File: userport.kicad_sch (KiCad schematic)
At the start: 43 parts, among them J3 C64_User_Port, J4 Mini-DIN-8-With-Shield, J5 C64_Tape_Port, J6 OKR-T/3-W12-C, U1 74LS595, U10 74LS125, U11 74LS595, U2 74LVC165, U3 74LS125, U4 74LS595, U5 74LVC165, U6 74LS595, U7 74LVC165, U8 74LS125, U9 74LS125

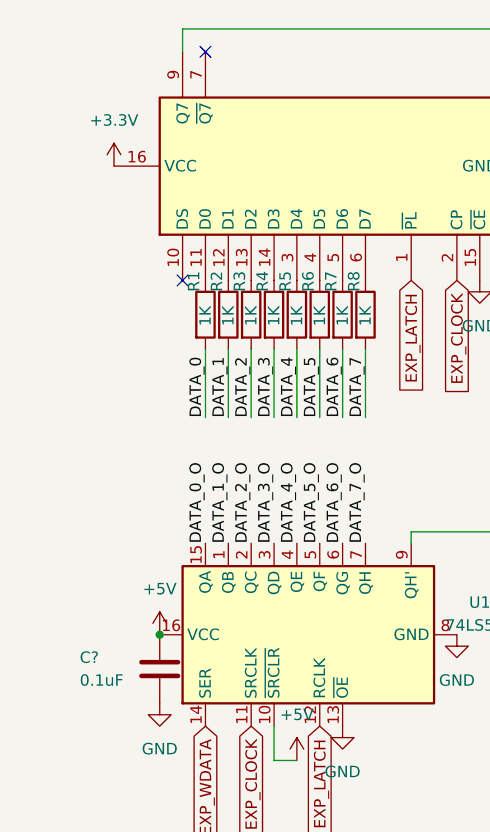
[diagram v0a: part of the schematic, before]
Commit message: add decoupling cap to U2
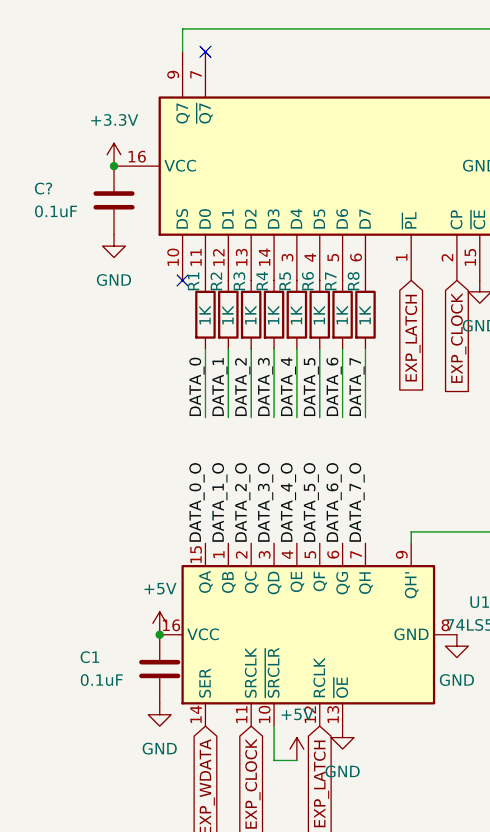
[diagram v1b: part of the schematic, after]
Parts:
- added C?: 0.1uF, Capacitor_THT:C_Disc_D5.0mm_W2.5mm_P5.00mm, symbol Device:C
- C1: renamed from C?; footprint Capacitor_THT:C_Disc_D10.0mm_W2.5mm_P5.00mm -> Capacitor_THT:C_Disc_D5.0mm_W2.5mm_P5.00mm
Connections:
- net +3V3: now also C?.1
- net GND: now also C?.2

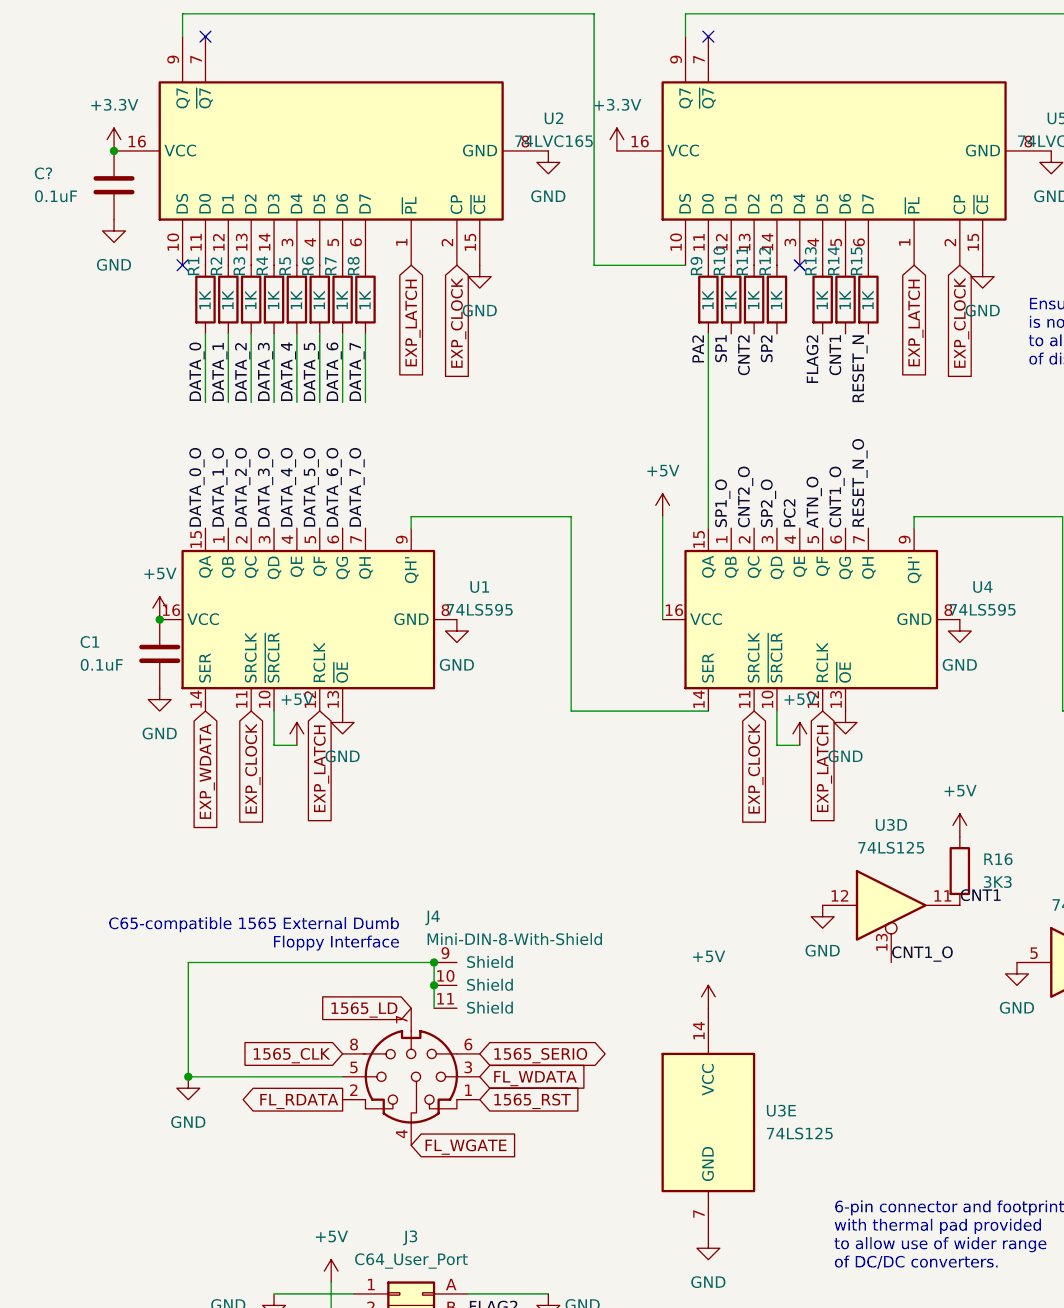
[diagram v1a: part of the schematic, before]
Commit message: add decoupling cap to U3
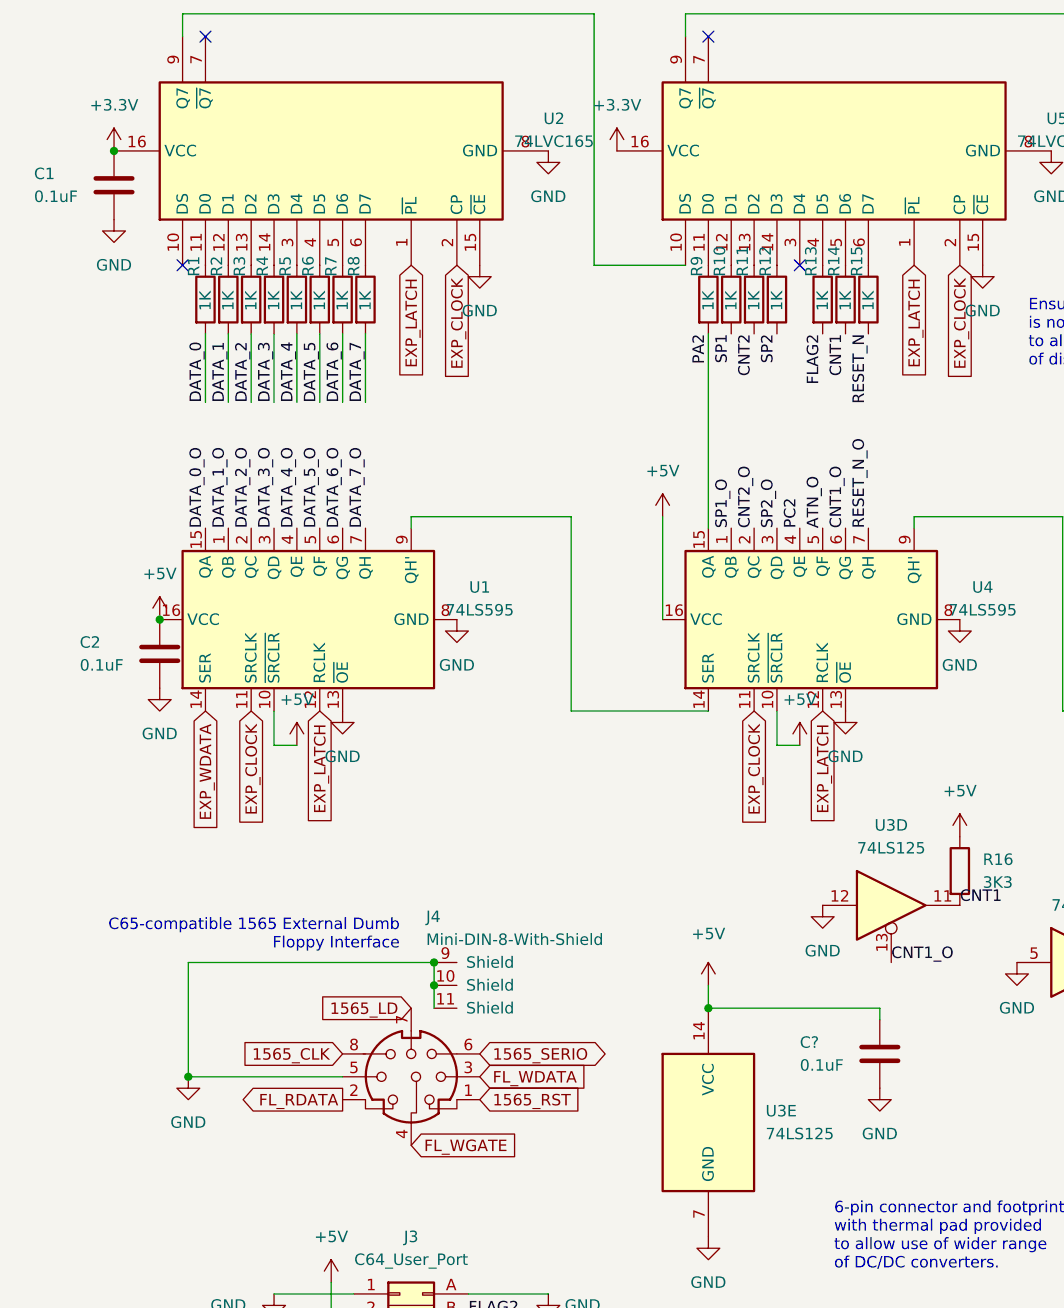
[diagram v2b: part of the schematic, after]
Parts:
- added C?: 0.1uF, Capacitor_THT:C_Disc_D5.0mm_W2.5mm_P5.00mm, symbol Device:C
- gave numbers to parts that had none: 1
- renumbered C1 to C2
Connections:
- net +5V: now also C?.1
- net GND: now also C?.2

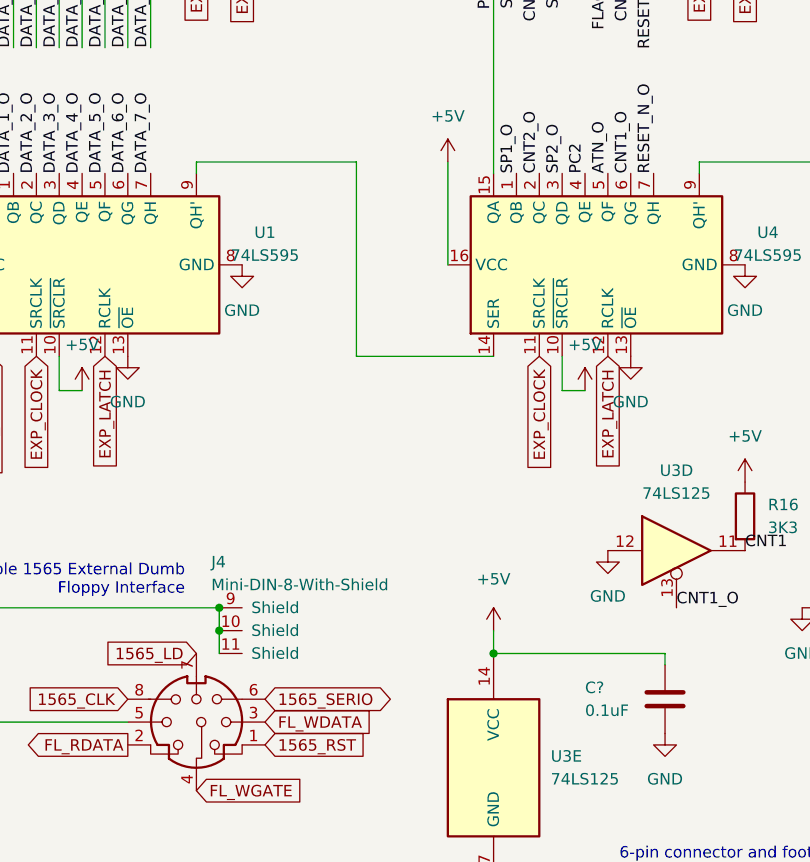
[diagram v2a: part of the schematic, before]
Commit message: add decoupling cap to U4
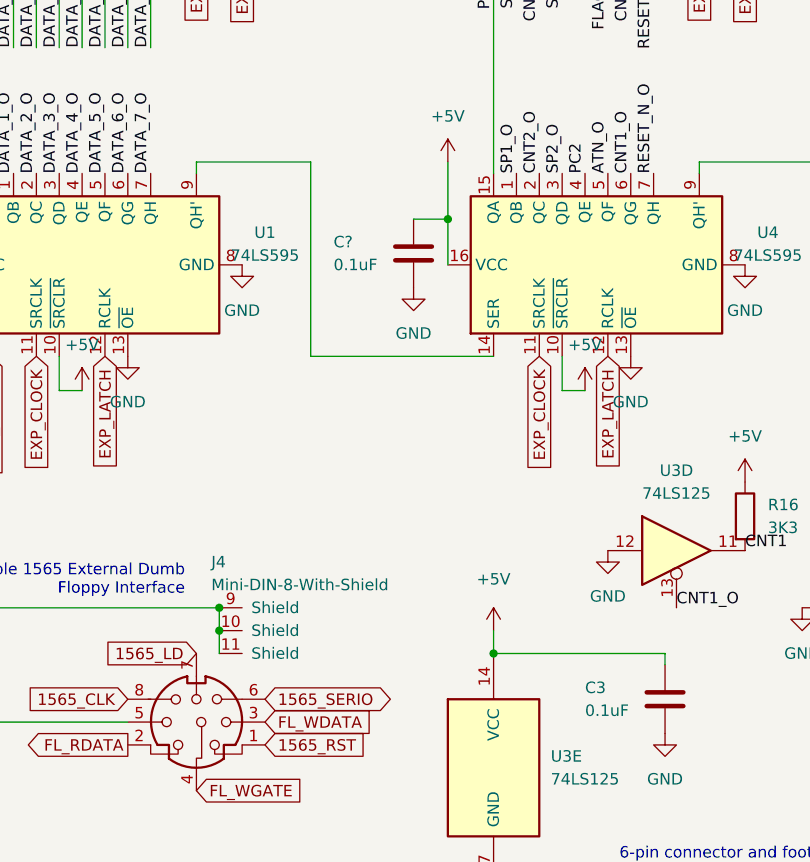
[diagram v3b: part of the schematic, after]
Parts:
- added C?: 0.1uF, Capacitor_THT:C_Disc_D5.0mm_W2.5mm_P5.00mm, symbol Device:C
- gave numbers to parts that had none: 1
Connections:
- net +5V: now also C?.1
- net GND: now also C?.2

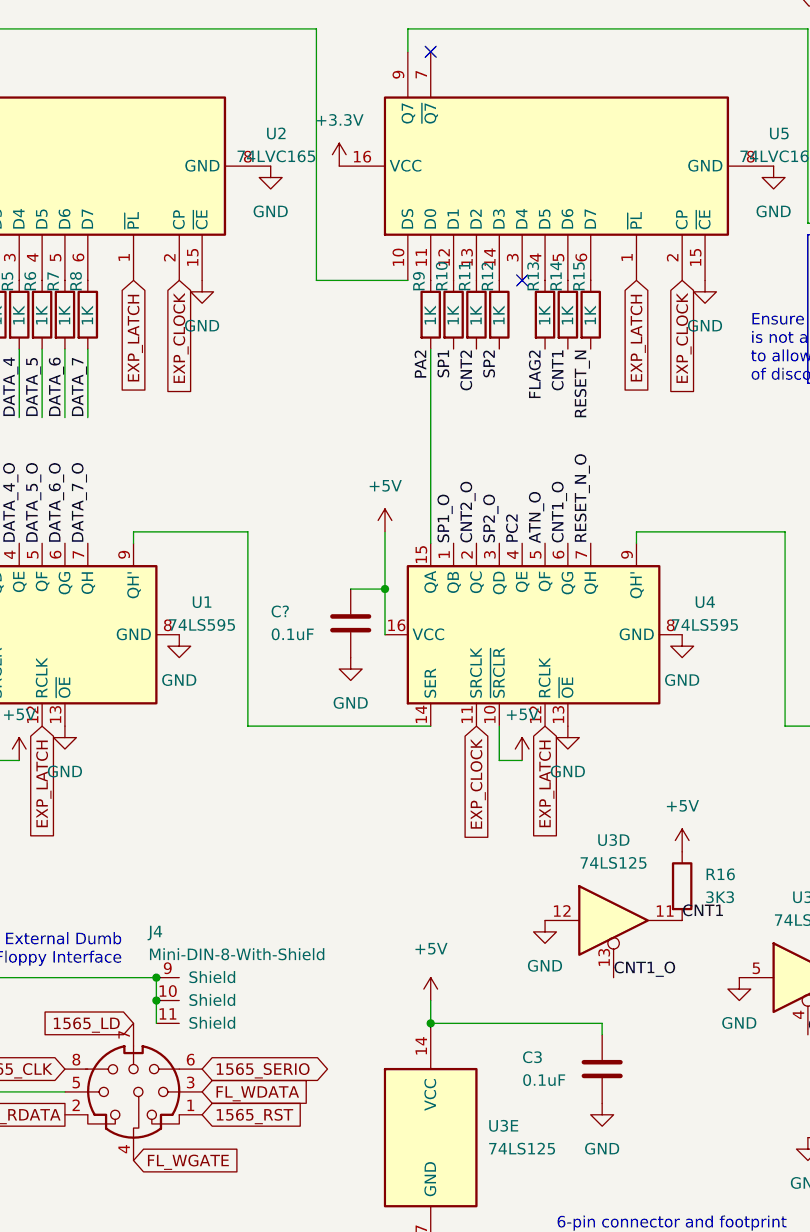
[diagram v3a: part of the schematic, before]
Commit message: add decoupling cap to U5
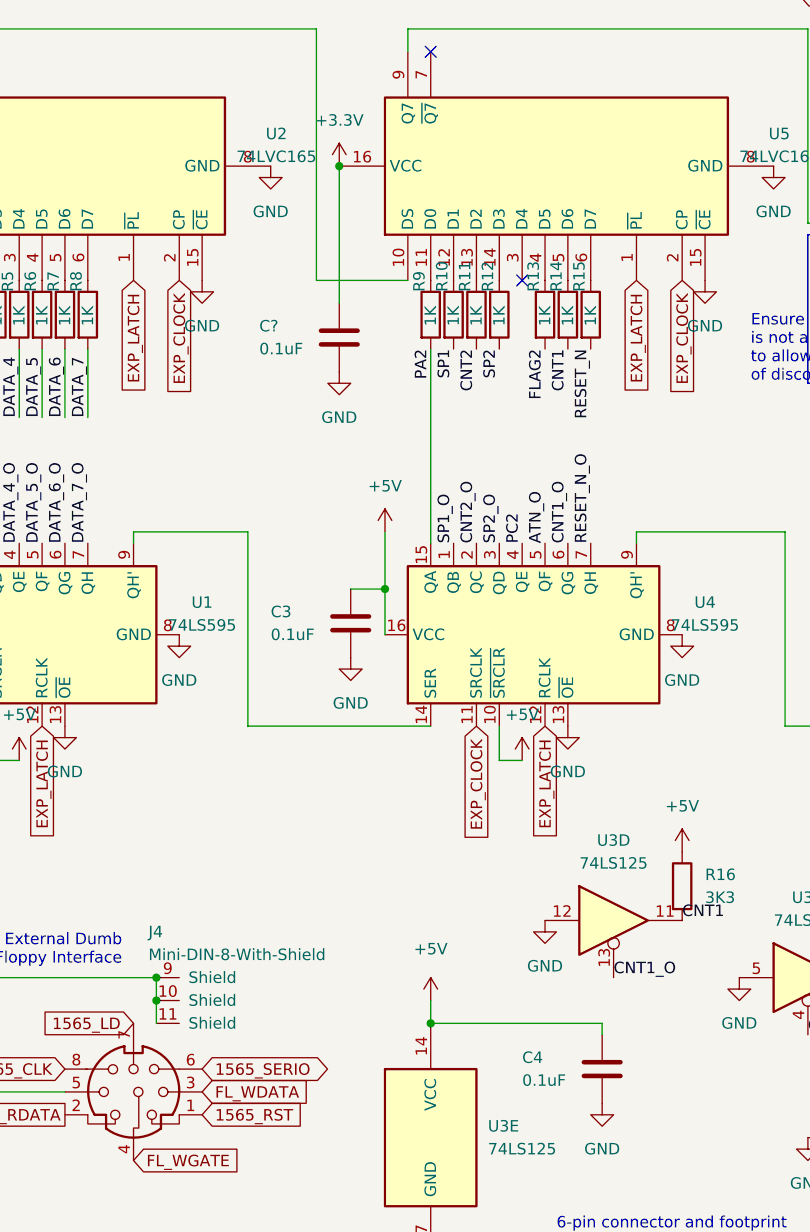
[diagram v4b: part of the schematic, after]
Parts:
- added C?: 0.1uF, Capacitor_THT:C_Disc_D5.0mm_W2.5mm_P5.00mm, symbol Device:C
- gave numbers to parts that had none: 1
- renumbered C3 to C4
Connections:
- net +3V3: now also C?.1
- net GND: now also C?.2

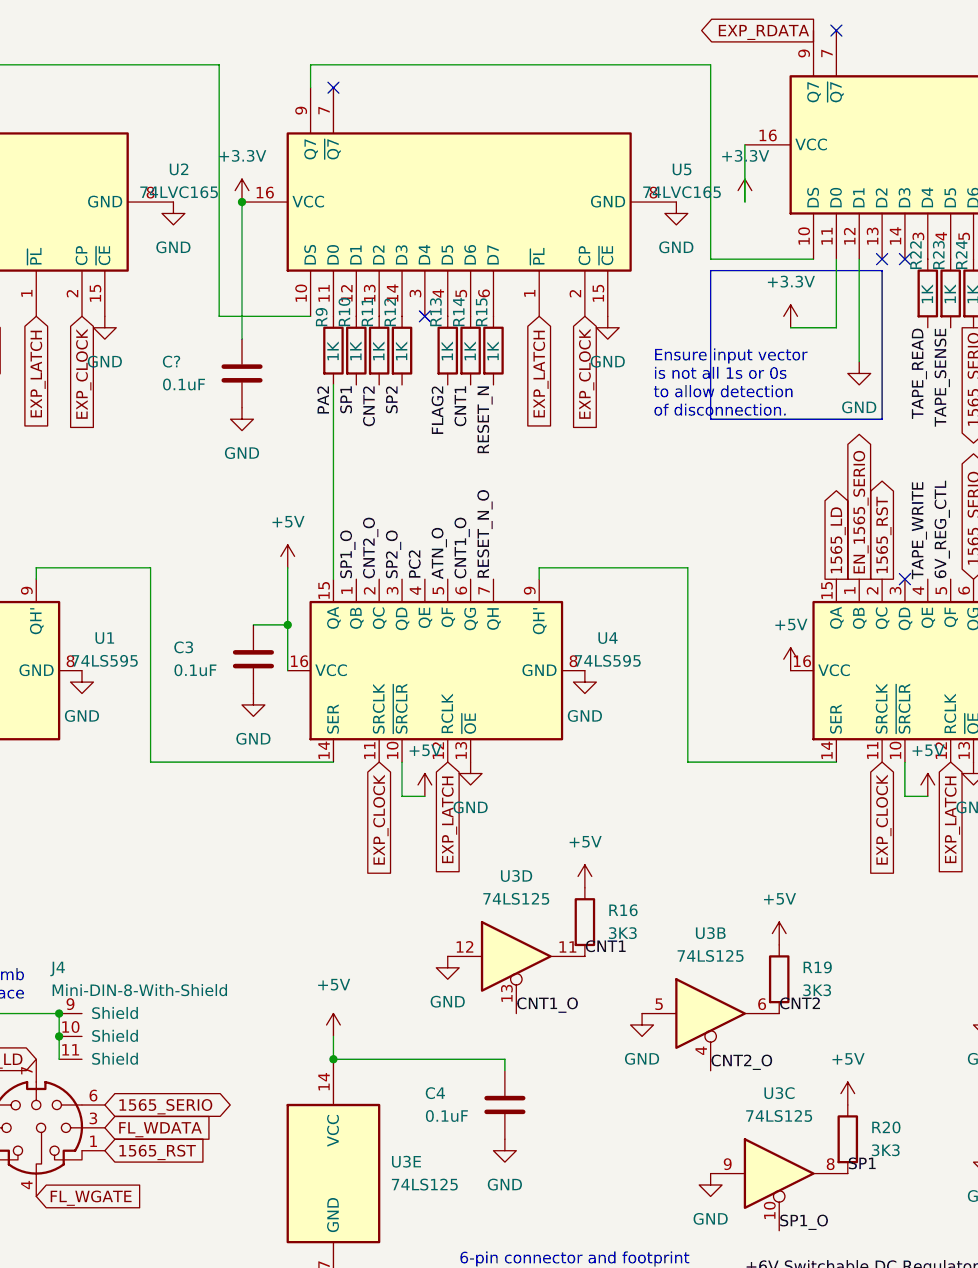
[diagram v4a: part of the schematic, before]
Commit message: add U6 and U7 decoupling caps
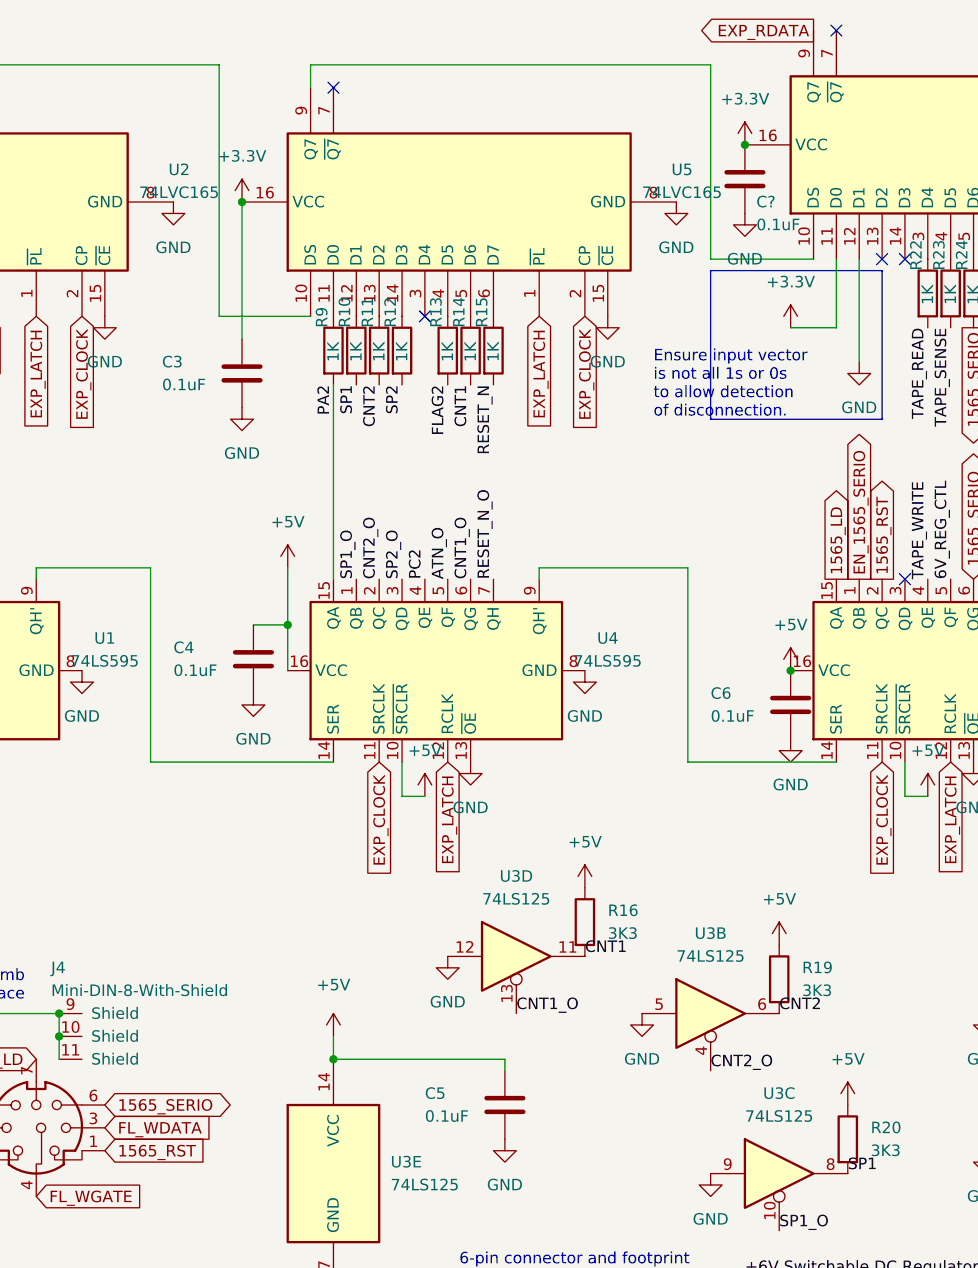
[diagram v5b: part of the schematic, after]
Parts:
- added C6, C?: 0.1uF, Capacitor_THT:C_Disc_D5.0mm_W2.5mm_P5.00mm, symbol Device:C
- gave numbers to parts that had none: 1
- renumbered C3 to C4, C4 to C5
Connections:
- net +3V3: now also C?.1
- net +5V: now also C6.1
- net GND: now also C6.2, C?.2
